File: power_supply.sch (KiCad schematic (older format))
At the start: 51 parts, among them IC1 TPS54561DPRT, J2 PJ-202A

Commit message: Modifications after P. Szczygiel review
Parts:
- removed C28, C? (x2): C_2u2_0402, sc606-baseboard-footprints:0402-cap, symbol sc606-baseboard:C_2u2_0402
- removed R4: R_10k_0402, sc606-baseboard-footprints:0402-res, symbol sc606-baseboard:R_10k_0402
- added C? (x3): C_10u_0402, antmicro-footprints:0402-cap, symbol antmicroCapacitors0402:C_10u_0402
- added D?: V8PM45-M3_H, sc606-baseboard-footprints:TO-277A, symbol sc606-baseboard:V8PM45-M3_H
- added R?: R_1M0_0402, antmicro-footprints:0402-res, symbol antmicroResistors0402:R_1M0_0402
- added R?: R_140k_0402, antmicro-footprints:0402-res, symbol antmicroResistors0402:R_140k_0402
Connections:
- wire segments 135 -> 136
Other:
- note added: "9...36 VDC"
- note added: "Inductor value differs from datasheet.\nIt is calculated and works."
- note added: "info: \nDrop voltage on one diode: 0.46V\nApprox. output voltage: 3.62V\nWith diodes temperature rise,\nvoltage dropout will decrease and output voltage increase"
- note removed: "info: \nDrop voltage on one diode: 0.46V\nApprox. output voltage: 4.08V"
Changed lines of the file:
@@
 F 1 "TPS54561DPRT" H 2800 5150 60  0000 L BNN
 F 2 "sc606-baseboard-footprints:WSON-10_4x4" H 3200 5850 60  0001 C CNN
-F 3 "" H 3200 5850 60  0001 C CNN
+F 3 "https://www.ti.com/lit/ds/symlink/tps54561.pdf?HQS=dis-dk-null-digikeymode-dsf-pf-null-wwe&ts=1642406709110&ref_url=https%253A%252F%252Fwww.ti.com%252Fgeneral%252Fdocs%252Fsuppproductinfo.tsp%253FdistId%253D10%2526gotoUrl%253Dhttps%253A%252F%252Fwww.ti.com%252Flit%252Fgpn%252Ftps54561" H 3200 5850 60  0001 C CNN
 F 4 "Texas Instrumets" H 3200 5850 50  0001 C CNN "Manufacturer"
 F 5 "TPS54561DPRT" H 3200 5850 50  0001 C CNN "MPN"
@@
 Wire Wire Line
 	10650 5350 10850 5350
-$Comp
-L sc606-baseboard:C_2u2_0402 C28
-U 1 1 61DDA18F
-P 10150 5750
-F 0 "C28" H 10265 5795 60  0000 L CNN
-F 1 "C_2u2_0402" H 10150 5600 60  0001 C CNN
-F 2 "sc606-baseboard-footprints:0402-cap" H 10350 5950 60  0001 L CNN
-F 3 "" H 10150 5750 50  0001 C CNN
-F 4 "TDK" H 10350 6150 60  0001 L CNN "Manufacturer"
-F 5 "C1005X5R1A225K050BC" H 10350 6050 60  0001 L CNN "MPN"
-F 6 "2u2" H 10265 5697 50  0000 L CNN "Val"
-	1    10150 5750
-	1    0    0    -1
-$EndComp
 Wire Wire Line
 	10150 5600 10150 5150
@@
 V_SOM
 Wire Wire Line
-	12600 2450 11600 2450
-Text Notes 10700 1750 0    50   ~ 0
-info: \nDrop voltage on one diode: 0.46V\nApprox. output voltage: 4.08V
+	12600 2450 12300 2450
+Text Notes 10500 1900 0    50   ~ 0
+info: \nDrop voltage on one diode: 0.46V\nApprox. output voltage: 3.62V\nWith diodes temperature rise,\nvoltage dropout will decrease and output voltage increase
 Text Notes 8600 7150 0    100  ~ 20
 5V to 3V3  DC/DC for camera\n\n
@@
 Wire Wire Line
 	9900 5350 10350 5350
-$Comp
-L sc606-baseboard:R_10k_0402 R4
-U 1 1 6204E79B
-P 2000 5650
-F 0 "R4" H 2000 5750 60  0000 C CNN
-F 1 "R_10k_0402" H 2000 5500 60  0001 C CNN
-F 2 "sc606-baseboard-footprints:0402-res" H 2200 5850 60  0001 L CNN
-F 3 "" H 2000 5650 50  0001 C CNN
-F 4 "VISHAY" H 2200 6050 60  0001 L CNN "Manufacturer"
-F 5 "CRCW040210K0FKEDHP" H 2200 5950 60  0001 L CNN "MPN"
-F 6 "10k" H 2000 5550 50  0000 C CNN "Val"
-	1    2000 5650
-	1    0    0    -1
-$EndComp
-Text GLabel 1450 5650 0    50   Input ~ 0
+Text GLabel 1000 5650 0    50   Input ~ 0
 #RESET
-Wire Wire Line
-	1450 5650 1850 5650
-Wire Wire Line
-	2600 5650 2150 5650
 Text Notes 2200 8300 0    100  ~ 20
 5V to 1V2 for Lontium9611\n
@@
 Wire Wire Line
 	10650 8100 10850 8100
-$Comp
-L sc606-baseboard:C_2u2_0402 C?
-U 1 1 62251E70
-P 10150 8500
-F 0 "C?" H 10265 8545 60  0000 L CNN
-F 1 "C_2u2_0402" H 10150 8350 60  0001 C CNN
-F 2 "sc606-baseboard-footprints:0402-cap" H 10350 8700 60  0001 L CNN
-F 3 "" H 10150 8500 50  0001 C CNN
-F 4 "TDK" H 10350 8900 60  0001 L CNN "Manufacturer"
-F 5 "C1005X5R1A225K050BC" H 10350 8800 60  0001 L CNN "MPN"
-F 6 "2u2" H 10265 8447 50  0000 L CNN "Val"
-	1    10150 8500
-	1    0    0    -1
-$EndComp
 Wire Wire Line
 	10150 8350 10150 7900
@@
 Wire Wire Line
 	2350 9650 2550 9650
-$Comp
-L sc606-baseboard:C_2u2_0402 C?
-U 1 1 62287E80
-P 1850 10050
-F 0 "C?" H 1965 10095 60  0000 L CNN
-F 1 "C_2u2_0402" H 1850 9900 60  0001 C CNN
-F 2 "sc606-baseboard-footprints:0402-cap" H 2050 10250 60  0001 L CNN
-F 3 "" H 1850 10050 50  0001 C CNN
-F 4 "TDK" H 2050 10450 60  0001 L CNN "Manufacturer"
-F 5 "C1005X5R1A225K050BC" H 2050 10350 60  0001 L CNN "MPN"
-F 6 "2u2" H 1965 9997 50  0000 L CNN "Val"
-	1    1850 10050
-	1    0    0    -1
-$EndComp
 Wire Wire Line
 	1850 9900 1850 9450
@@
 	0    1    1    0
 $EndComp
+Text Notes 4050 1750 0    50   ~ 0
+9...36 VDC
+$Comp
+L antmicroCapacitors0402:C_10u_0402 C?
+U 1 1 620BC82F
+P 10150 5750
+F 0 "C?" H 10265 5795 60  0000 L CNN
+F 1 "C_10u_0402" H 10150 5600 60  0001 C CNN
+F 2 "antmicro-footprints:0402-cap" H 10350 5950 60  0001 L CNN
+F 3 "" H 10150 5750 50  0001 C CNN
+F 4 "YAGEO" H 10350 6150 60  0001 L CNN "Manufacturer"
+F 5 "CC0402MRX5R5BB106" H 10350 6050 60  0001 L CNN "MPN"
+F 6 "10u" H 10265 5697 50  0000 L CNN "Val"
+	1    10150 5750
+	1    0    0    -1
+$EndComp
+$Comp
+L antmicroCapacitors0402:C_10u_0402 C?
+U 1 1 620BCB1C
+P 10150 8500
+F 0 "C?" H 10265 8545 60  0000 L CNN
+F 1 "C_10u_0402" H 10150 8350 60  0001 C CNN
+F 2 "antmicro-footprints:0402-cap" H 10350 8700 60  0001 L CNN
+F 3 "" H 10150 8500 50  0001 C CNN
+F 4 "YAGEO" H 10350 8900 60  0001 L CNN "Manufacturer"
+F 5 "CC0402MRX5R5BB106" H 10350 8800 60  0001 L CNN "MPN"
+F 6 "10u" H 10265 8447 50  0000 L CNN "Val"
+	1    10150 8500
+	1    0    0    -1
+$EndComp
+$Comp
+L antmicroCapacitors0402:C_10u_0402 C?
+U 1 1 620C69F9
+P 1850 10050
+F 0 "C?" H 1965 10095 60  0000 L CNN
+F 1 "C_10u_0402" H 1850 9900 60  0001 C CNN
+F 2 "antmicro-footprints:0402-cap" H 2050 10250 60  0001 L CNN
+F 3 "" H 1850 10050 50  0001 C CNN
+F 4 "YAGEO" H 2050 10450 60  0001 L CNN "Manufacturer"
+F 5 "CC0402MRX5R5BB106" H 2050 10350 60  0001 L CNN "MPN"
+F 6 "10u" H 1965 9997 50  0000 L CNN "Val"
+	1    1850 10050
+	1    0    0    -1
+$EndComp
+Text Notes 3650 9050 0    50   ~ 0
+Inductor value differs from datasheet.\nIt is calculated and works.
+$Comp
+L sc606-baseboard:VCC #PWR?
+U 1 1 620D943B
+P 1250 5200
+F 0 "#PWR?" H 1250 5050 50  0001 C CNN
+F 1 "VCC" H 1250 5350 50  0000 C CNN
+F 2 "" H 1250 5200 50  0001 C CNN
+F 3 "" H 1250 5200 50  0001 C CNN
+	1    1250 5200
+	1    0    0    -1
+$EndComp
+$Comp
+L sc606-baseboard:GND #PWR?
+U 1 1 620D98F4
+P 1250 6100
+F 0 "#PWR?" H 1250 5850 50  0001 C CNN
+F 1 "GND" H 1250 5950 50  0000 C CNN
+F 2 "" H 1250 6100 50  0001 C CNN
+F 3 "" H 1250 6100 50  0001 C CNN
+	1    1250 6100
+	1    0    0    -1
+$EndComp
+$Comp
+L antmicroResistors0402:R_1M0_0402 R?
+U 1 1 620DF4A0
+P 1250 5350
+F 0 "R?" V 1205 5420 60  0000 L CNN
+F 1 "R_1M0_0402" H 1250 5200 60  0001 C CNN
+F 2 "antmicro-footprints:0402-res" H 1450 5550 60  0001 L CNN
+F 3 "" H 1250 5350 50  0001 C CNN
+F 4 "TE CONNECTIVITY" H 1450 5750 60  0001 L CNN "Manufacturer"
+F 5 "CRG0402F1M0" H 1450 5650 60  0001 L CNN "MPN"
+F 6 "1M0" V 1303 5420 50  0000 L CNN "Val"
+	1    1250 5350
+	0    1    1    0
+$EndComp
+$Comp
+L antmicroResistors0402:R_140k_0402 R?
+U 1 1 620E03B8
+P 1250 5950
+F 0 "R?" V 1205 6020 60  0000 L CNN
+F 1 "R_140k_0402" H 1250 5800 60  0001 C CNN
+F 2 "antmicro-footprints:0402-res" H 1450 6150 60  0001 L CNN
+F 3 "" H 1250 5950 50  0001 C CNN
+F 4 "Yageo" H 1450 6350 60  0001 L CNN "Manufacturer"
+F 5 "RC0402FR-07140KL" H 1450 6250 60  0001 L CNN "MPN"
+F 6 "140k" V 1303 6020 50  0000 L CNN "Val"
+	1    1250 5950
+	0    1    1    0
+$EndComp
+Wire Wire Line
+	1000 5650 2600 5650
+Wire Wire Line
+	1250 5500 1250 5800
+$Comp
+L sc606-baseboard:V8PM45-M3_H D?
+U 1 1 621043D7
+P 12100 2450
+F 0 "D?" H 12100 2712 60  0000 C CNN
+F 1 "V8PM45-M3_H" H 12100 2606 60  0000 C CNN
+F 2 "sc606-baseboard-footprints:TO-277A" H 12300 2650 60  0001 L CNN
+F 3 "https://pl.mouser.com/datasheet/2/427/VISH_S_A0006899224_1-2570035.pdf" H 12300 2750 60  0001 L CNN
+F 4 "V8PM45-M3/H" H 12300 2950 60  0001 L CNN "MPN"
+F 5 "VISHAY" H 12300 3550 60  0001 L CNN "Manufacturer"
+	1    12100 2450
+	1    0    0    -1
+$EndComp
+Wire Wire Line
+	11900 2450 11600 2450
 $EndSCHEMATC

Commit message: Added corrections to schemas after review
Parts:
- removed R11, R? (x2): R_10k_0402, sc606-baseboard-footprints:0402-res, symbol sc606-baseboard:R_10k_0402
- removed R?: R_1M0_0402, antmicro-footprints:0402-res, symbol antmicroResistors0402:R_1M0_0402
- removed R?: R_140k_0402, antmicro-footprints:0402-res, symbol antmicroResistors0402:R_140k_0402
- added Q?: BSS138APW, antmicro-footprints:SC70-3, symbol antmicroTransistorsFETsMOSFETsSingle:BSS138APW
- added R?: R_120k_0402, antmicro-footprints:0402-res, symbol antmicroResistors0402:R_120k_0402
- added R?: R_18k_0402, antmicro-footprints:0402-res, symbol antmicroResistors0402:R_18k_0402
- added R? (x3): R_0R_0402, antmicro-footprints:0402-res, symbol antmicroResistors0402:R_0R_0402
- added R? (x3): R_100k_0402, antmicro-footprints:0402-res, symbol antmicroResistors0402:R_100k_0402
- added R?: R_100R_0402, antmicro-footprints:0402-res, symbol antmicroResistors0402:R_100R_0402
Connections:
- net labels added: CAM_RST
- net labels removed: #RESET
- wire segments 136 -> 155
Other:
- moved on the sheet: C?

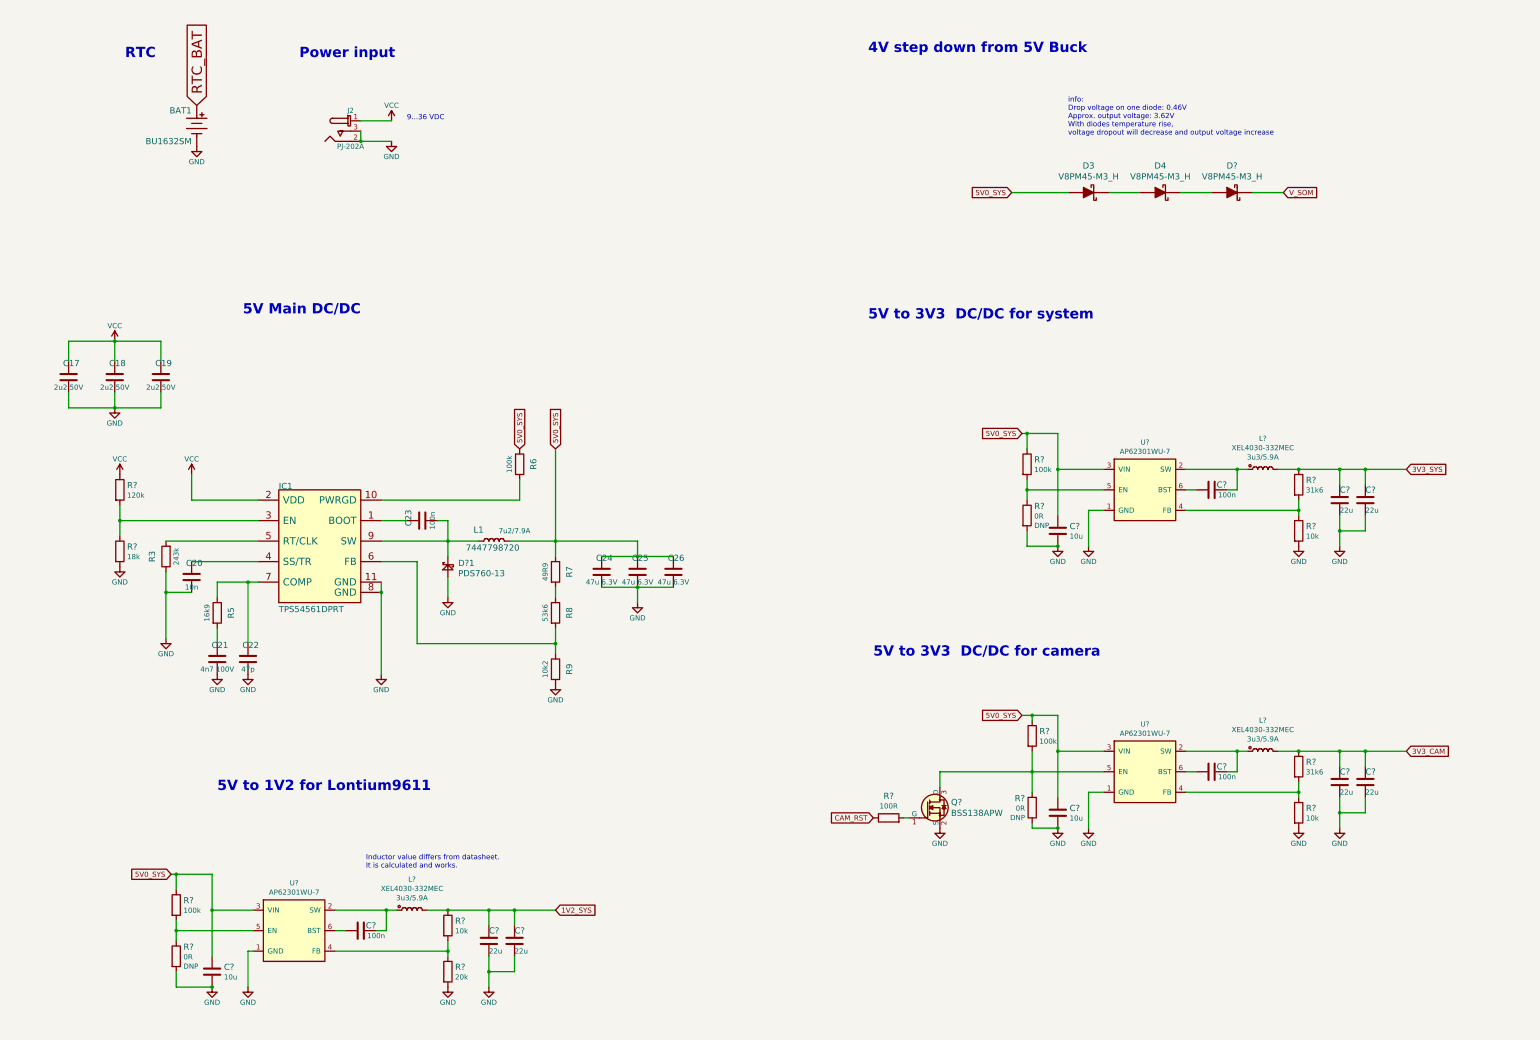
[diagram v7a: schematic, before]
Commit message: Added Auto-On circuit in power_supply.sch
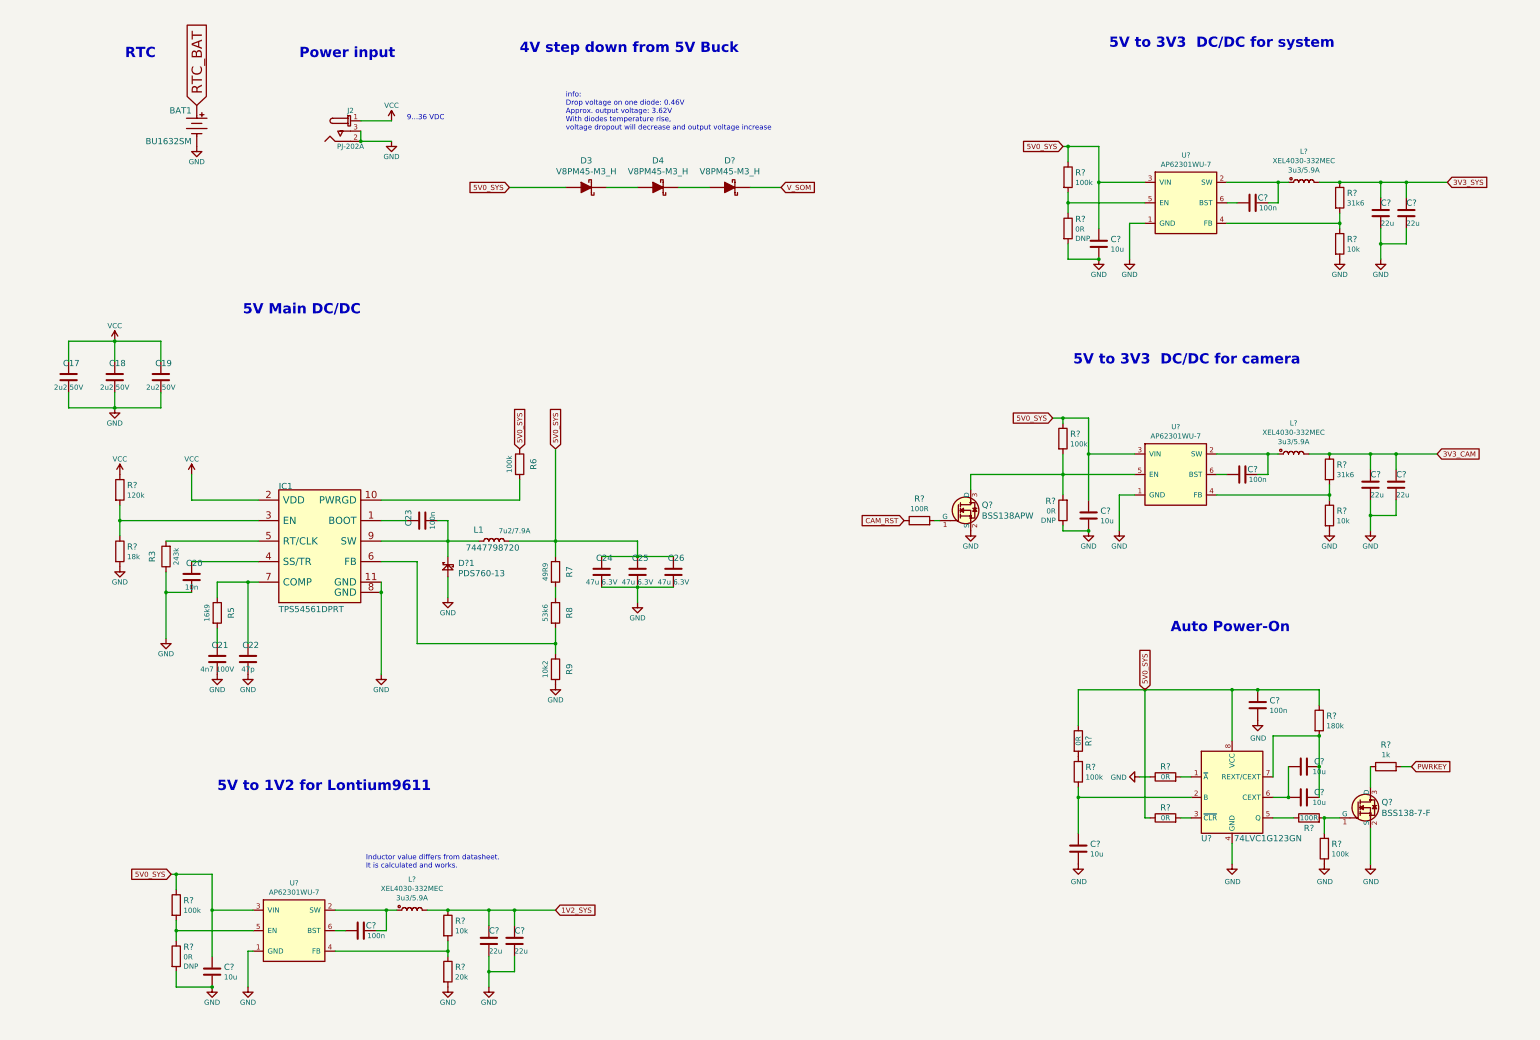
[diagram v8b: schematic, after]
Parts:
- added C?: C_100n_0402, sc606-baseboard-footprints:0402-cap, symbol sc606-baseboard:C_100n_0402
- added C? (x3): C_10u_0402, antmicro-footprints:0402-cap, symbol antmicroCapacitors0402:C_10u_0402
- added Q?: BSS138-7-F, antmicro-footprints:SOT-23-3, symbol antmicroTransistorsFETsMOSFETsSingle:BSS138-7-F
- added R?: R_1k_0402, antmicro-footprints:0402-res, symbol antmicroResistors0402:R_1k_0402
- added R?: R_100R_0402, antmicro-footprints:0402-res, symbol antmicroResistors0402:R_100R_0402
- added R? (x2): R_100k_0402, antmicro-footprints:0402-res, symbol antmicroResistors0402:R_100k_0402
- added R?: R_180k_0402, antmicro-footprints:0402-res, symbol antmicroResistors0402:R_180k_0402
- added R? (x3): R_0R_0402, antmicro-footprints:0402-res, symbol antmicroResistors0402:R_0R_0402
- added U?: 74LVC1G123GN, sc606-baseboard-footprints:XSON8-SOT1116, symbol sc606-baseboard:74LVC1G123GN
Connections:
- net 5V0_SYS: now also C?.2, R?.1, R?.1, R?.1, U?.8 (VCC)
- net GND: now also C?.1, C?.2, Q?.2 (S), R?.1, R?.1, U?.4 (GND)
- new net: Q?.1 (G), R?.2, R?.2
- new net: Q?.3 (D), R?.1
- new net: R?.1, U?.5 (Q)
- new net: R?.2, U?.1 (~A)
- new net: C?.1, R?.1, U?.2 (B)
- new net: R?.2, U?.3 (~CLR)
- new net: C?.1, C?.1, U?.6 (CEXT)
- new net: C?.2, C?.2, R?.2, U?.7 (REXT/CEXT)
- new net: R?.2, R?.2
- new net PWRKEY: R?.2
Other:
- note added: "Auto Power-On"
- moved on the sheet: C?, D3, D4, D?, L?, Q?, R?, U?
